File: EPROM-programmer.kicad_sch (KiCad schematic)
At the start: 24 parts, among them J1 ZIF-socket, J2 ISP, P1 USB-C, SW1 SW_Push, U1 ATmega1284-P, U2 MCP2221AxP, Y1 20M

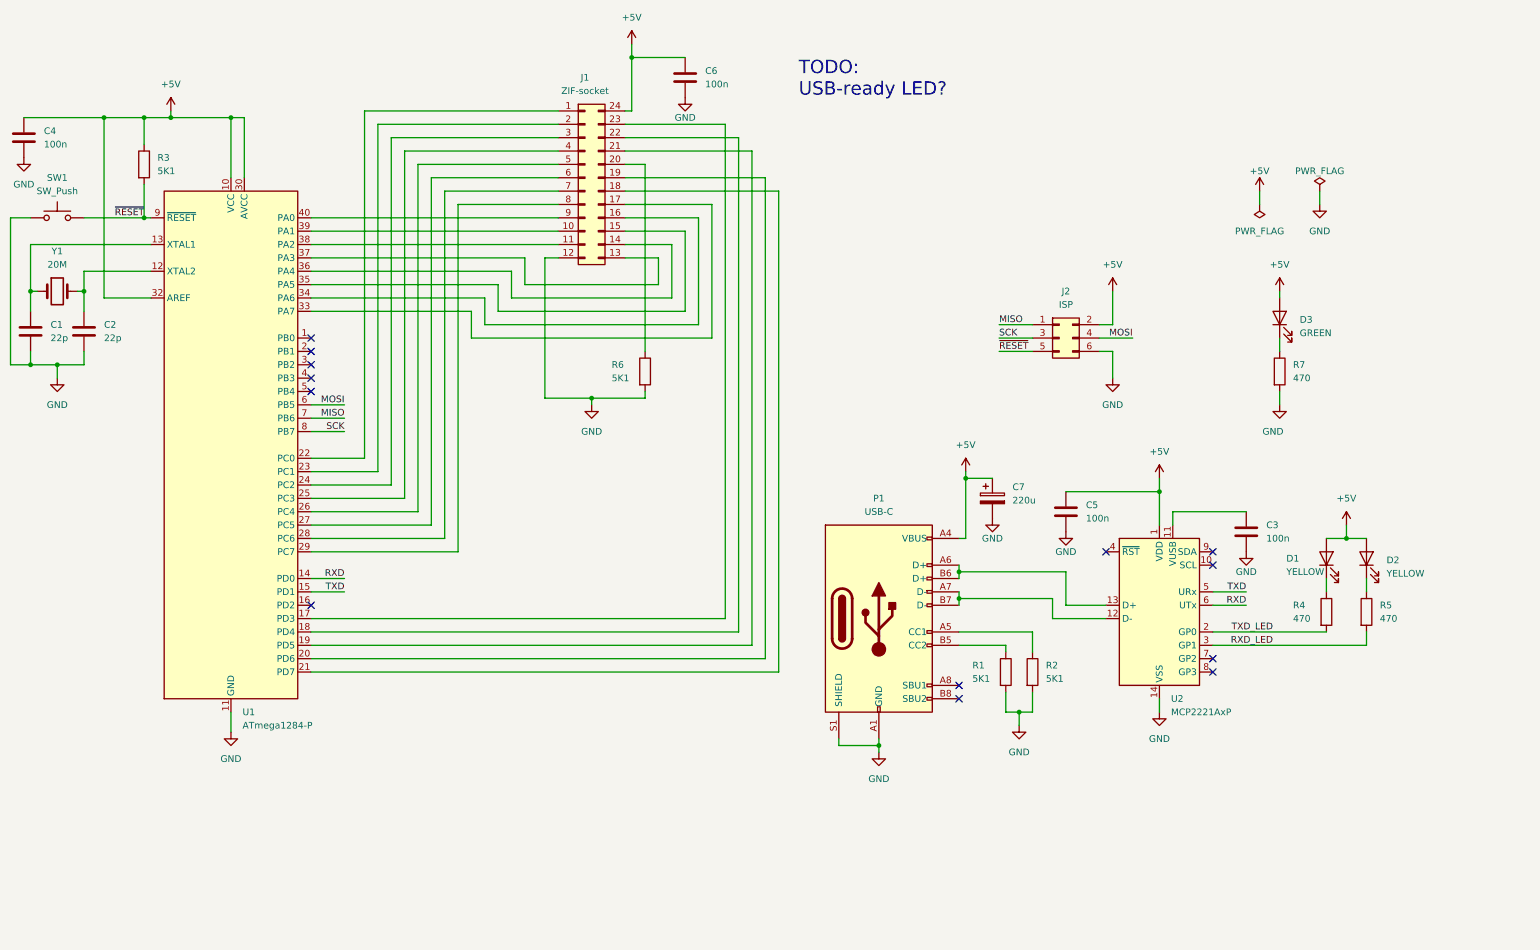
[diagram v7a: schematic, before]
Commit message: Add DAC and more
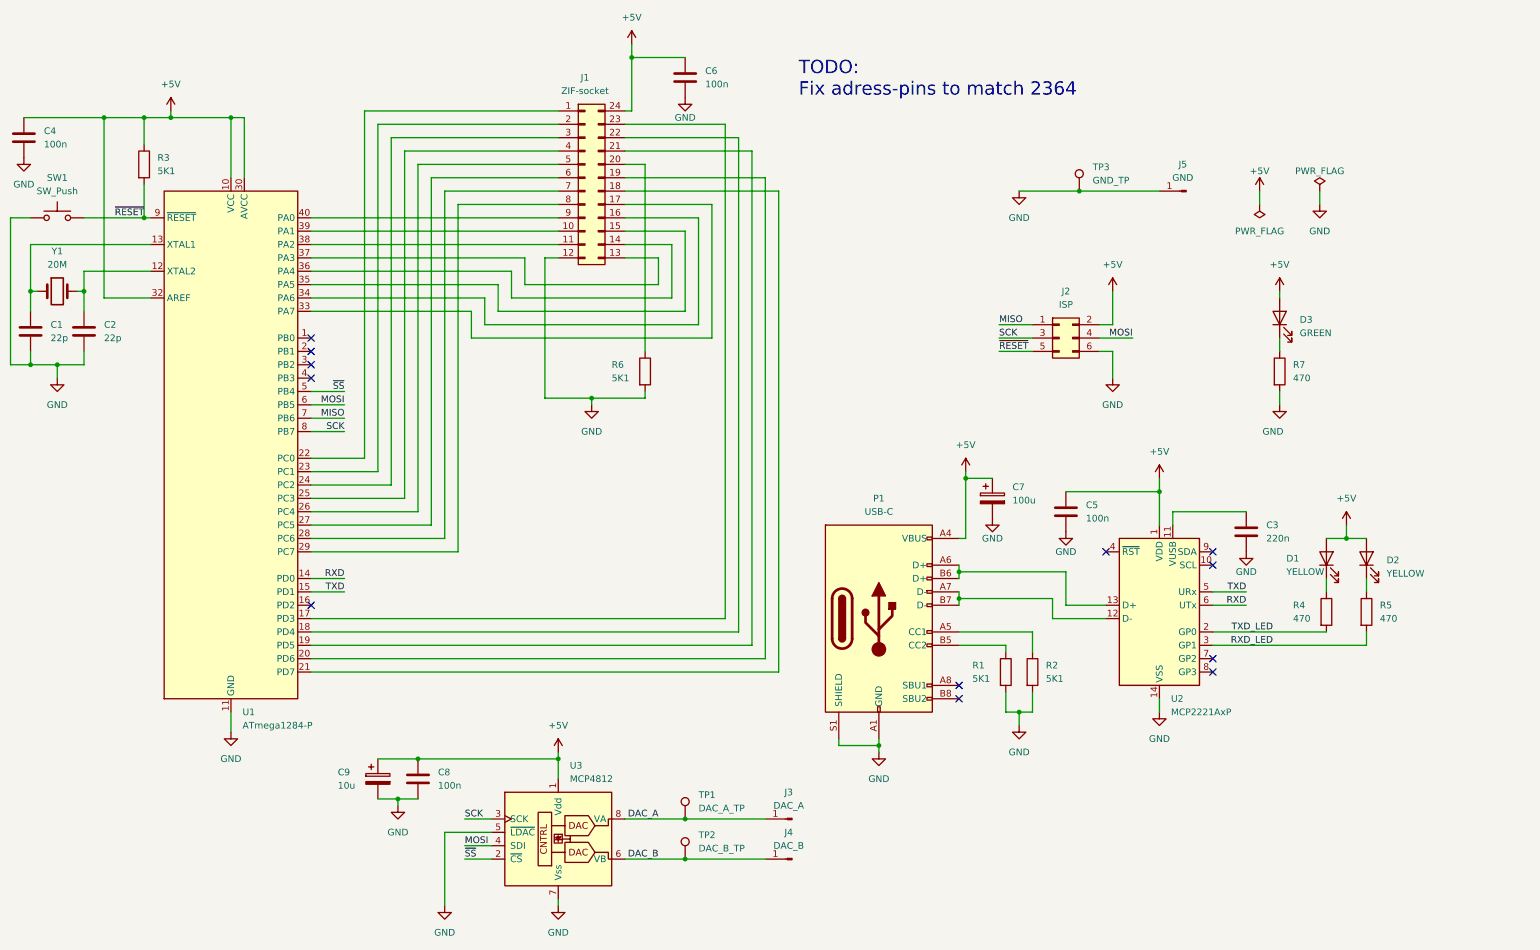
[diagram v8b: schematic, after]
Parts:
- added C8: 100n, Capacitor_THT:C_Rect_L4.6mm_W3.0mm_P2.50mm_MKS02_FKP02, symbol Device:C
- added C9: 10u, symbol Device:C_Polarized
- added J3: DAC_A, Connector_PinHeader_2.54mm:PinHeader_1x01_P2.54mm_Vertical, symbol Connector:Conn_01x01_Pin
- added J4: DAC_B, Connector_PinHeader_2.54mm:PinHeader_1x01_P2.54mm_Vertical, symbol Connector:Conn_01x01_Pin
- added J5: GND, Connector_PinHeader_2.54mm:PinHeader_1x01_P2.54mm_Vertical, symbol Connector:Conn_01x01_Pin
- added TP1: DAC_A_TP, TestPoint:TestPoint_Pad_2.0x2.0mm, symbol Connector:TestPoint
- added TP2: DAC_B_TP, TestPoint:TestPoint_Pad_2.0x2.0mm, symbol Connector:TestPoint
- added TP3: GND_TP, TestPoint:TestPoint_Pad_2.0x2.0mm, symbol Connector:TestPoint
- added U3: MCP4812, Package_DIP:DIP-8_W7.62mm, symbol Analog_DAC:MCP4812
- C3: value 100n -> 220n
- C7: value 220u -> 100u
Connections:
- net +5V: now also C8.1, C9.1, U3.1 (Vdd)
- net GND: now also C8.2, C9.2, J5.1 (Pin_1), TP3.1, U3.5 (~{LDAC}), U3.7 (Vss)
- net MOSI: now also U3.4 (SDI)
- net SCK: now also U3.3 (SCK)
- net ~{SS}: now reaches U1.5 (PB4)
- net ~{SS}: now also U3.2 (~{CS})
- new net DAC_A: J3.1 (Pin_1), TP1.1, U3.8 (VA)
- new net DAC_B: J4.1 (Pin_1), TP2.1, U3.6 (VB)
- no-connect marks 13 -> 12
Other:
- note added: "TODO: Fix adress-pins to match 2364"
- note removed: "TODO: USB-ready LED?"
